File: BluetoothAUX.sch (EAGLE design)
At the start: 29 parts, among them IC1 NE5532D, X2 MINI-USB-SCHIELD-32005-201, X3 STEREOJACK

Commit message: Add trimmers
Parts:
- removed JP9: SPEAKER, pinhead:PINHD-1X3
- removed R5, R6: 10K, rcl:R-EU_R0805
- added R12, R14: (no value), resistor:R-TRIMM3314G
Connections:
- net GND: no longer JP9.2
- net N$1: now also R12.A; no longer R5.1
- net N$10: now also R14.S; no longer R6.2
- net N$3: now also R14.A; no longer R6.1
- net N$9: now also R12.S; no longer R5.2
- net SPK_L: no longer JP9.1
- net SPK_R: no longer JP9.3
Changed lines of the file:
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@@
 <part name="C3" library="rcl" deviceset="C-EU" device="C0805" value="1uF"/>
 <part name="C4" library="rcl" deviceset="C-EU" device="C0805" value="1uF"/>
-<part name="R5" library="rcl" deviceset="R-EU_" device="R0805" value="10K"/>
-<part name="R6" library="rcl" deviceset="R-EU_" device="R0805" value="10K"/>
 <part name="C5" library="rcl" deviceset="C-EU" device="C0805" value="1uF"/>
 <part name="C6" library="rcl" deviceset="C-EU" device="C0805" value="1uF"/>
@@
 <part name="GND6" library="supply1" deviceset="GND" device=""/>
 <part name="GND7" library="supply1" deviceset="GND" device=""/>
-<part name="JP9" library="pinhead" library_urn="urn:adsk.eagle:library:325" deviceset="PINHD-1X3" device="" package3d_urn="urn:adsk.eagle:package:22458/2" value="SPEAKER"/>
-<part name="GND8" library="supply1" deviceset="GND" device=""/>
 <part name="JP10" library="pinhead" library_urn="urn:adsk.eagle:library:325" deviceset="PINHD-1X8" device="" package3d_urn="urn:adsk.eagle:package:22409/2" value="PROG"/>
 <part name="X3" library="adafruit" deviceset="STEREOJACK" device=""/>
@@
 <part name="X2" library="con-cypressindustries" library_urn="urn:adsk.eagle:library:138" deviceset="MINI-USB-SCHIELD-" device="32005-201" package3d_urn="urn:adsk.eagle:package:6443/1"/>
 <part name="GND10" library="supply1" deviceset="GND" device=""/>
+<part name="R12" library="resistor" library_urn="urn:adsk.eagle:library:348" deviceset="R-TRIMM" device="3314G" package3d_urn="urn:adsk.eagle:package:26056/1"/>
+<part name="R14" library="resistor" library_urn="urn:adsk.eagle:library:348" deviceset="R-TRIMM" device="3314G" package3d_urn="urn:adsk.eagle:package:26056/1"/>
 </parts>
 <sheets>
@@
 <instance part="C3" gate="G$1" x="7.62" y="20.32" rot="R90"/>
 <instance part="C4" gate="G$1" x="7.62" y="10.16" rot="R90"/>
-<instance part="R5" gate="G$1" x="58.42" y="104.14"/>
-<instance part="R6" gate="G$1" x="50.8" y="-5.08"/>
 <instance part="C5" gate="G$1" x="81.28" y="86.36" rot="R90"/>
 <instance part="C6" gate="G$1" x="81.28" y="12.7" rot="R90"/>
@@
 <instance part="GND6" gate="1" x="-157.48" y="60.96"/>
 <instance part="GND7" gate="1" x="-147.32" y="-12.7"/>
-<instance part="JP9" gate="A" x="124.46" y="48.26"/>
-<instance part="GND8" gate="1" x="109.22" y="40.64"/>
 <instance part="JP10" gate="A" x="-180.34" y="17.78" rot="R180"/>
 <instance part="X3" gate="1" x="154.94" y="50.8"/>
@@
 <instance part="X2" gate="S" x="-142.24" y="66.04"/>
 <instance part="GND10" gate="1" x="-139.7" y="55.88"/>
+<instance part="R12" gate="G$1" x="58.42" y="104.14" rot="R270"/>
+<instance part="R14" gate="G$1" x="50.8" y="-5.08" rot="R270"/>
 </instances>
 <busses>
@@
 <wire x1="35.56" y1="88.9" x2="35.56" y2="104.14" width="0.1524" layer="91"/>
 <junction x="35.56" y="88.9"/>
-<pinref part="R5" gate="G$1" pin="1"/>
 <wire x1="35.56" y1="104.14" x2="53.34" y2="104.14" width="0.1524" layer="91"/>
+<pinref part="R12" gate="G$1" pin="A"/>
 </segment>
 </net>
@@
 <wire x1="35.56" y1="10.16" x2="35.56" y2="-5.08" width="0.1524" layer="91"/>
 <junction x="35.56" y="10.16"/>
-<pinref part="R6" gate="G$1" pin="1"/>
 <wire x1="35.56" y1="-5.08" x2="45.72" y2="-5.08" width="0.1524" layer="91"/>
+<pinref part="R14" gate="G$1" pin="A"/>
 </segment>
 </net>
@@
 <pinref part="IC1" gate="A" pin="OUT"/>
 <wire x1="58.42" y1="86.36" x2="68.58" y2="86.36" width="0.1524" layer="91"/>
-<wire x1="68.58" y1="86.36" x2="68.58" y2="104.14" width="0.1524" layer="91"/>
-<pinref part="R5" gate="G$1" pin="2"/>
-<wire x1="68.58" y1="104.14" x2="63.5" y2="104.14" width="0.1524" layer="91"/>
+<wire x1="68.58" y1="86.36" x2="68.58" y2="96.52" width="0.1524" layer="91"/>
 <pinref part="C5" gate="G$1" pin="1"/>
 <wire x1="68.58" y1="86.36" x2="78.74" y2="86.36" width="0.1524" layer="91"/>
 <junction x="68.58" y="86.36"/>
+<pinref part="R12" gate="G$1" pin="S"/>
+<wire x1="58.42" y1="99.06" x2="58.42" y2="96.52" width="0.1524" layer="91"/>
+<wire x1="58.42" y1="96.52" x2="68.58" y2="96.52" width="0.1524" layer="91"/>
 </segment>
 </net>
 <net name="N$10" class="0">
 <segment>
+<pinref part="R14" gate="G$1" pin="S"/>
+<wire x1="50.8" y1="-10.16" x2="50.8" y2="-12.7" width="0.1524" layer="91"/>
+<wire x1="50.8" y1="-12.7" x2="68.58" y2="-12.7" width="0.1524" layer="91"/>
+<wire x1="68.58" y1="-12.7" x2="68.58" y2="12.7" width="0.1524" layer="91"/>
+<pinref part="C6" gate="G$1" pin="1"/>
 <pinref part="IC1" gate="B" pin="OUT"/>
 <wire x1="58.42" y1="12.7" x2="68.58" y2="12.7" width="0.1524" layer="91"/>
-<wire x1="68.58" y1="12.7" x2="68.58" y2="-5.08" width="0.1524" layer="91"/>
-<pinref part="R6" gate="G$1" pin="2"/>
-<wire x1="68.58" y1="-5.08" x2="55.88" y2="-5.08" width="0.1524" layer="91"/>
-<pinref part="C6" gate="G$1" pin="1"/>
 <wire x1="68.58" y1="12.7" x2="78.74" y2="12.7" width="0.1524" layer="91"/>
 <junction x="68.58" y="12.7"/>
@@
 <pinref part="C5" gate="G$1" pin="2"/>
 <label x="114.3" y="86.36" size="1.778" layer="95" xref="yes"/>
-<pinref part="JP9" gate="A" pin="1"/>
-<wire x1="121.92" y1="50.8" x2="114.3" y2="50.8" width="0.1524" layer="91"/>
-<wire x1="114.3" y1="50.8" x2="114.3" y2="63.5" width="0.1524" layer="91"/>
 <wire x1="114.3" y1="63.5" x2="114.3" y2="86.36" width="0.1524" layer="91"/>
 <wire x1="114.3" y1="86.36" x2="86.36" y2="86.36" width="0.1524" layer="91"/>
 <wire x1="114.3" y1="63.5" x2="137.16" y2="63.5" width="0.1524" layer="91"/>
 <wire x1="137.16" y1="63.5" x2="137.16" y2="53.34" width="0.1524" layer="91"/>
-<junction x="114.3" y="63.5"/>
 <pinref part="X3" gate="1" pin="5"/>
 <wire x1="137.16" y1="53.34" x2="142.24" y2="53.34" width="0.1524" layer="91"/>
@@
 <wire x1="86.36" y1="12.7" x2="114.3" y2="12.7" width="0.1524" layer="91"/>
 <wire x1="114.3" y1="12.7" x2="114.3" y2="25.4" width="0.1524" layer="91"/>
-<pinref part="JP9" gate="A" pin="3"/>
-<wire x1="114.3" y1="25.4" x2="114.3" y2="45.72" width="0.1524" layer="91"/>
-<wire x1="114.3" y1="45.72" x2="121.92" y2="45.72" width="0.1524" layer="91"/>
 <wire x1="114.3" y1="25.4" x2="137.16" y2="25.4" width="0.1524" layer="91"/>
 <wire x1="137.16" y1="25.4" x2="137.16" y2="45.72" width="0.1524" layer="91"/>
-<junction x="114.3" y="25.4"/>
 <pinref part="X3" gate="1" pin="2"/>
 <wire x1="137.16" y1="45.72" x2="142.24" y2="45.72" width="0.1524" layer="91"/>
@@
 </segment>
 <segment>
-<pinref part="JP9" gate="A" pin="2"/>
-<wire x1="121.92" y1="48.26" x2="109.22" y2="48.26" width="0.1524" layer="91"/>
-<wire x1="109.22" y1="48.26" x2="109.22" y2="43.18" width="0.1524" layer="91"/>
-<pinref part="GND8" gate="1" pin="GND"/>
-</segment>
-<segment>

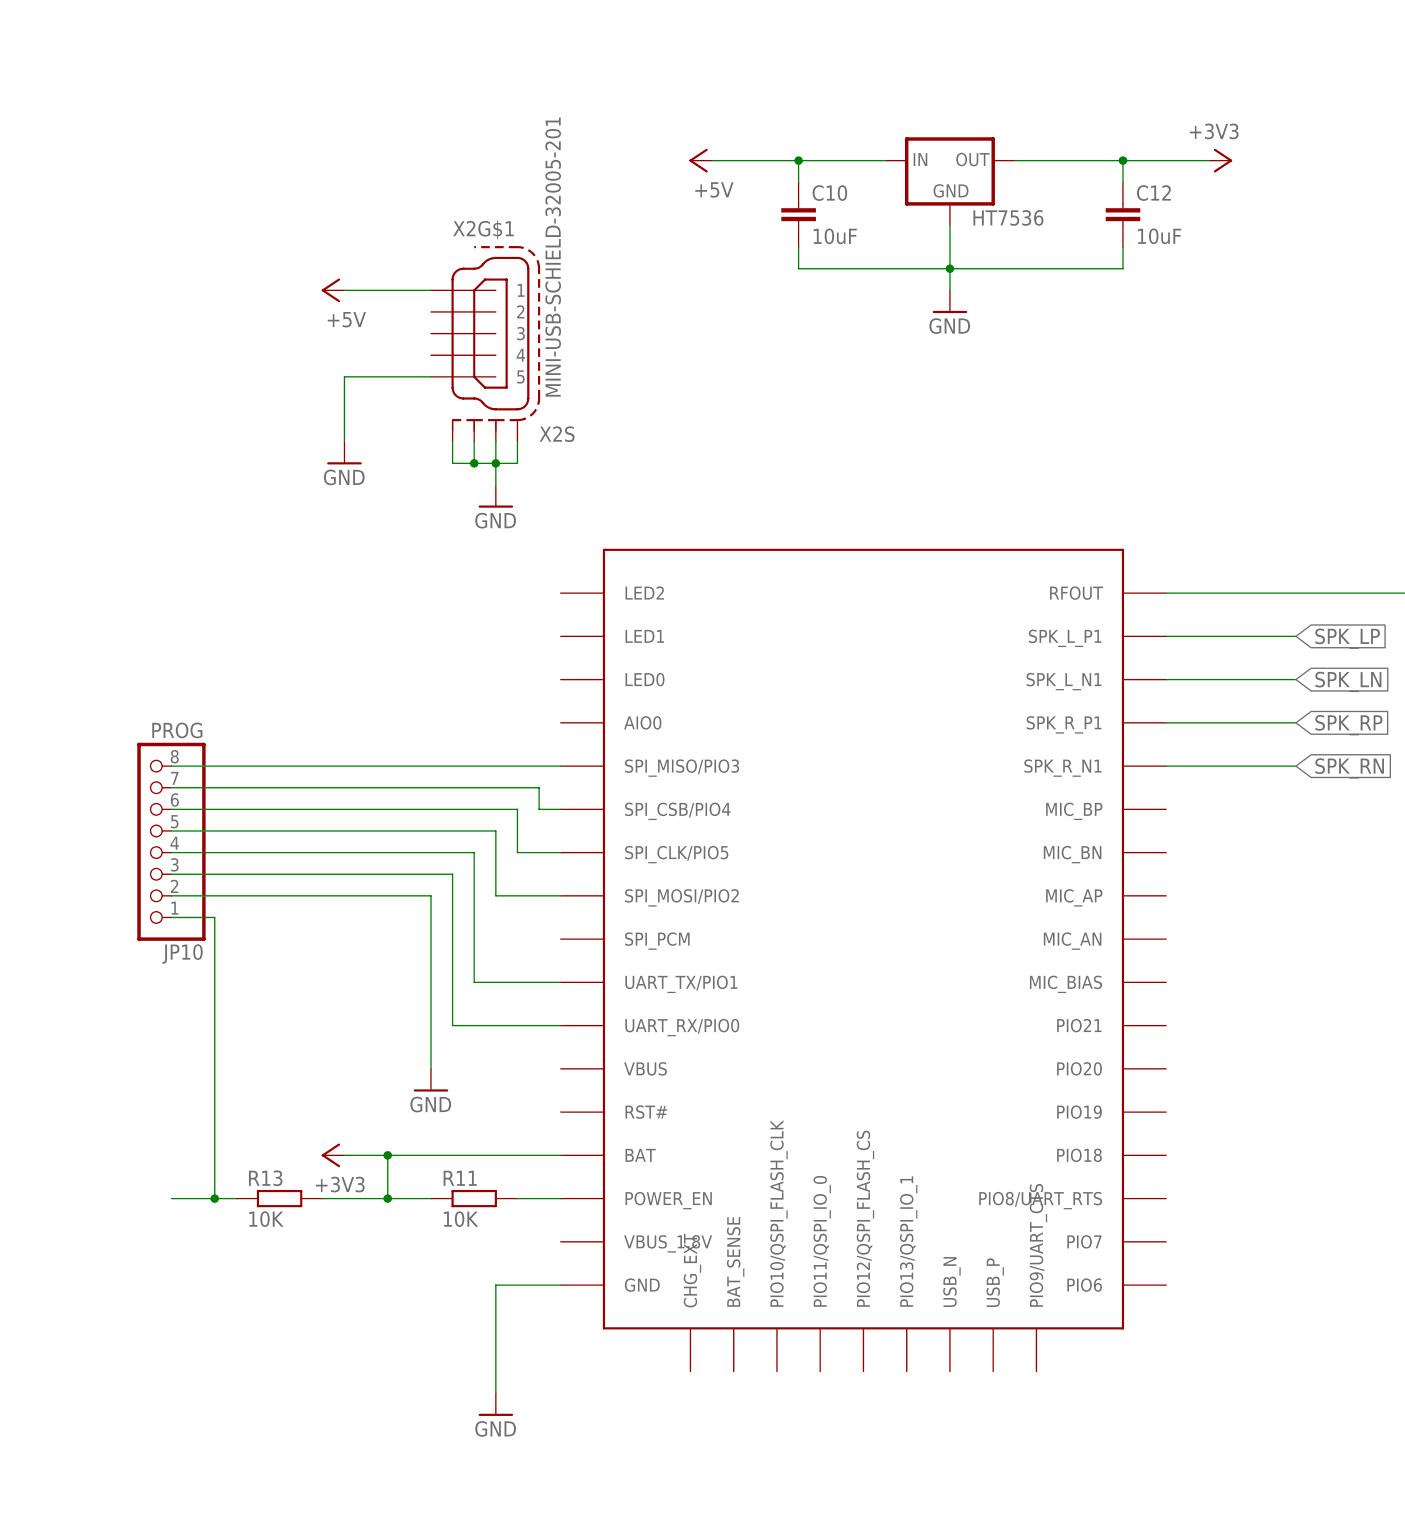
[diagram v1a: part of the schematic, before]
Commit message: Drop DCDC for direct USB supply
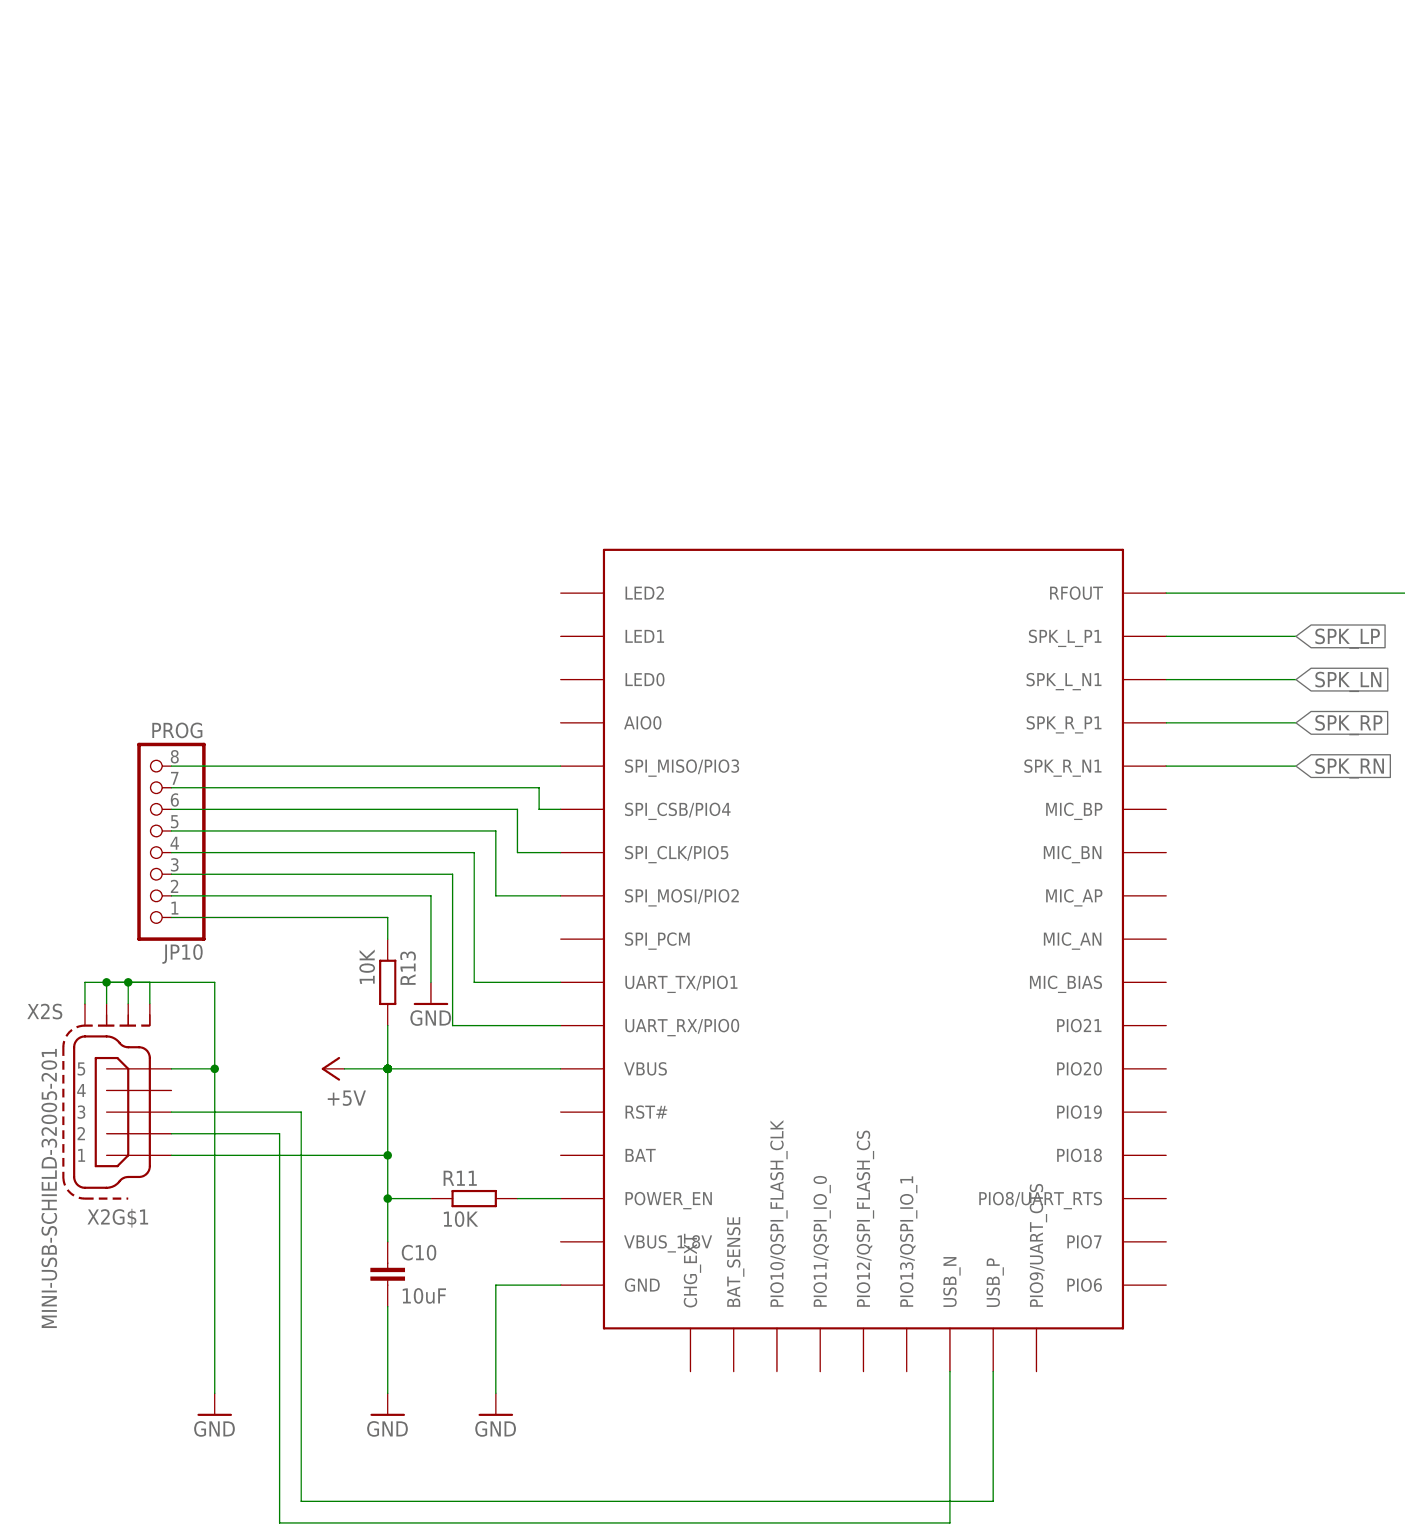
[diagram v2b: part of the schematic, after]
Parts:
- removed C12: 10uF, rcl:C-EUC1206
- removed HT7536: 7536, BT:7536
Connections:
- removed net +3V3: C12.1, HT7536.OUT, R11.1, R13.2, U$1.BAT
- new net N$18: U$1.USB_N, X2G$1.2
- new net N$19: U$1.USB_P, X2G$1.3
- net +5V: now also R11.1, R13.2, U$1.VBUS; no longer HT7536.IN
- net GND: no longer C12.2, HT7536.GND
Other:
- moved on the sheet: C10, R13, X2G$1, X2S

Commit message: TPA6132A
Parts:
- removed C10: 10uF, rcl:C-EUC1206
- removed C6: 1uF, rcl:C-EUC0805
- removed C7: 4.7uF, rcl:C-EUC0805
- removed C8: 10nF, rcl:C-EUC0805
- removed IC1: NE5532D, BT:NE5532D
- removed R10, R9: 100K, rcl:R-EU_R0805
- removed R11, R13, R4, R7, R8: 10K, rcl:R-EU_R0805
- removed R12, R14: (no value), resistor:R-TRIMM3314G
- removed X3: STEREOJACK, adafruit:STEREOJACK
- added IC2: TPA6132A2, texas:TPA6132A2
- added RN1: CTS742C083, resistor-net:CTS742C083
- added X1: STEREOJACK, adafruit:STEREOJACK
- C1, C3: device rcl:C-EUC0805 -> resistor:C-EUC0603
- C2, C4: value 1uF -> 2.2uF; device rcl:C-EUC0805 -> resistor:C-EUC0603
- C5: value 1uF -> 10uF; device rcl:C-EUC0805 -> rcl:C-EUC1206
- R1: device rcl:R-EU_R0805 -> resistor:R-EU_R0603
- R2, R3: value 10K -> (none); device rcl:R-EU_R0805 -> resistor:R-EU_R0603
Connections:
- removed net N$1: IC1A.-IN, R1.2, R12.A
- removed net N$10: C6.1, IC1B.OUT, R14.S
- removed net N$11: C7.1, C8.1, R10.2, R7.1, R8.2, R9.1
- removed net N$2: IC1A.+IN, R2.2, R7.2
- removed net N$3: IC1B.-IN, R14.A, R4.2
- removed net N$4: IC1B.+IN, R3.2, R8.1
- removed net N$5: C1.2, R1.1
- removed net N$6: C2.2, R2.1
- removed net N$7: C3.2, R3.1
- removed net N$8: C4.2, R4.1
- removed net N$9: C5.1, IC1A.OUT, R12.S
- removed net SPK_L: C5.2, X3.5
- removed net SPK_R: C6.2, X3.2
- new net N$14: IC2.OUTR, X1.2
- new net N$20: IC2.OUTL, X1.5
- new net N$26: C3.1, IC2.CPP
- new net N$27: C3.2, IC2.CPN
- new net N$28: C1.1, IC2.HPVSS
- new net N$29: C2.1, IC2.HPVDD
- new net N$30: IC2.EN, R1.1
- new net N$31: IC2.GO, R3.2, RN1.6
- new net N$32: IC2.G1, R2.2, RN1.5
- new net SGND: IC2.SGND, X1.1
- net +5V: now also C4.1, C5.1, IC2.VDD, R1.2, RN1.1, RN1.2, RN1.3, RN1.4; no longer C10.1, IC1P.V+, R11.1, R13.2, R9.2
- net COM: now also RN1.8; no longer R13.1
- net GND: now also C1.2, C2.2, C4.2, C5.2, IC2.PGND, R2.1, R3.1; no longer C10.2, C7.2, C8.2, IC1P.V-, R10.1, X3.1
- net N$13: now also RN1.7; no longer R11.2
- net SPK_LN: now also IC2.INL-; no longer C1.1
- net SPK_LP: now also IC2.INL+; no longer C2.1
- net SPK_RN: now also IC2.INR-; no longer C4.1
- net SPK_RP: now also IC2.INR+; no longer C3.1
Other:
- moved on the sheet: C1, C2, C3, C4, C5, R1, R2, R3

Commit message: LEDs
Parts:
- added LED1, LED2: (no value), led:LED3MM
- added RN2: 1K, resistor-net:CTS742C083
- RN1: value CTS742C083 -> 10K
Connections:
- new net LED1+: LED1.C, U$1.LED0
- new net LED1-: LED1.A, RN2.7
- new net LED2+: LED2.C, U$1.LED1
- new net LED2-: LED2.A, RN2.8
- net GND: now also RN2.1, RN2.2, RN2.3, RN2.4
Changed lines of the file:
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@@
 <part name="C3" library="resistor" library_urn="urn:adsk.eagle:library:348" deviceset="C-EU" device="C0603" package3d_urn="urn:adsk.eagle:package:26138/1" value="1uF"/>
 <part name="R1" library="resistor" library_urn="urn:adsk.eagle:library:348" deviceset="R-EU_" device="R0603" package3d_urn="urn:adsk.eagle:package:26057/1" value="10K"/>
-<part name="RN1" library="resistor-net" library_urn="urn:adsk.eagle:library:343" deviceset="CTS742C083" device="" package3d_urn="urn:adsk.eagle:package:24985/1"/>
+<part name="RN1" library="resistor-net" library_urn="urn:adsk.eagle:library:343" deviceset="CTS742C083" device="" package3d_urn="urn:adsk.eagle:package:24985/1" value="10K"/>
 <part name="C4" library="resistor" library_urn="urn:adsk.eagle:library:348" deviceset="C-EU" device="C0603" package3d_urn="urn:adsk.eagle:package:26138/1" value="2.2uF"/>
 <part name="GND1" library="supply1" deviceset="GND" device=""/>
+<part name="LED2" library="led" library_urn="urn:adsk.eagle:library:259" deviceset="LED" device="3MM" package3d_urn="urn:adsk.eagle:package:15797/1"/>
+<part name="LED1" library="led" library_urn="urn:adsk.eagle:library:259" deviceset="LED" device="3MM" package3d_urn="urn:adsk.eagle:package:15797/1"/>
+<part name="RN2" library="resistor-net" library_urn="urn:adsk.eagle:library:343" deviceset="CTS742C083" device="" package3d_urn="urn:adsk.eagle:package:24985/1" value="1K"/>
+<part name="GND2" library="supply1" deviceset="GND" device=""/>
 </parts>
 <sheets>
@@
 <instance part="C4" gate="G$1" x="48.26" y="17.78"/>
 <instance part="GND1" gate="1" x="48.26" y="7.62"/>
+<instance part="LED2" gate="G$1" x="-139.7" y="40.64" rot="R90"/>
+<instance part="LED1" gate="G$1" x="-147.32" y="35.56" rot="R90"/>
+<instance part="RN2" gate="G$1" x="-162.56" y="38.1"/>
+<instance part="GND2" gate="1" x="-190.5" y="27.94"/>
 </instances>
 <busses>
@@
 <wire x1="48.26" y1="12.7" x2="48.26" y2="10.16" width="0.1524" layer="91"/>
 </segment>
+<segment>
+<pinref part="RN2" gate="G$1" pin="1"/>
+<wire x1="-170.18" y1="33.02" x2="-170.18" y2="35.56" width="0.1524" layer="91"/>
+<wire x1="-170.18" y1="35.56" x2="-170.18" y2="38.1" width="0.1524" layer="91"/>
+<wire x1="-170.18" y1="38.1" x2="-170.18" y2="40.64" width="0.1524" layer="91"/>
+<wire x1="-170.18" y1="40.64" x2="-167.64" y2="40.64" width="0.1524" layer="91"/>
+<pinref part="RN2" gate="G$1" pin="2"/>
+<wire x1="-167.64" y1="38.1" x2="-170.18" y2="38.1" width="0.1524" layer="91"/>
+<junction x="-170.18" y="38.1"/>
+<pinref part="RN2" gate="G$1" pin="3"/>
+<wire x1="-167.64" y1="35.56" x2="-170.18" y2="35.56" width="0.1524" layer="91"/>
+<junction x="-170.18" y="35.56"/>
+<pinref part="RN2" gate="G$1" pin="4"/>
+<wire x1="-167.64" y1="33.02" x2="-170.18" y2="33.02" width="0.1524" layer="91"/>
+<wire x1="-170.18" y1="33.02" x2="-190.5" y2="33.02" width="0.1524" layer="91"/>
+<junction x="-170.18" y="33.02"/>
+<pinref part="GND2" gate="1" pin="GND"/>
+<wire x1="-190.5" y1="33.02" x2="-190.5" y2="30.48" width="0.1524" layer="91"/>
+</segment>
 </net>
 <net name="+5V" class="1">
@@
 </segment>
 </net>
+<net name="LED2-" class="0">
+<segment>
+<pinref part="RN2" gate="G$1" pin="8"/>
+<pinref part="LED2" gate="G$1" pin="A"/>
+<wire x1="-154.94" y1="40.64" x2="-142.24" y2="40.64" width="0.1524" layer="91"/>
+</segment>
+</net>
+<net name="LED1-" class="0">
+<segment>
+<pinref part="RN2" gate="G$1" pin="7"/>
+<wire x1="-154.94" y1="38.1" x2="-152.4" y2="38.1" width="0.1524" layer="91"/>
+<wire x1="-152.4" y1="38.1" x2="-152.4" y2="35.56" width="0.1524" layer="91"/>
+<pinref part="LED1" gate="G$1" pin="A"/>
+<wire x1="-152.4" y1="35.56" x2="-149.86" y2="35.56" width="0.1524" layer="91"/>
+</segment>
+</net>
+<net name="LED2+" class="0">
+<segment>
+<pinref part="LED2" gate="G$1" pin="C"/>
+<pinref part="U$1" gate="G$1" pin="LED1"/>
+<wire x1="-134.62" y1="40.64" x2="-132.08" y2="40.64" width="0.1524" layer="91"/>
+</segment>
+</net>
+<net name="LED1+" class="0">
+<segment>
+<pinref part="LED1" gate="G$1" pin="C"/>
+<pinref part="U$1" gate="G$1" pin="LED0"/>
+<wire x1="-142.24" y1="35.56" x2="-132.08" y2="35.56" width="0.1524" layer="91"/>
+</segment>
+</net>
